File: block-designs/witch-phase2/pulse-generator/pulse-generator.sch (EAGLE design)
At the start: 87 parts, among them IC1 74LVC1G17DBV, IC10 74LVC1G08DBV, IC11 74LVC1G08DBV, IC12 741G175, IC13 741G175, IC14 741G175, IC15 741G175, IC16 741G175, IC17 74LVC1G04DBV, IC18 74LVC1G04DBV, IC19 74LVC1G08DBV, IC2 74LVC1G17DBV, IC20 74LVC1G04DBV, IC21 74LVC1G08DBV, IC22 741G175, IC23 74LVC1G08DBV, IC3 74LVC1G17DBV, IC4 NE555D, IC5 741G175, IC6 74LVC1G04DBV, IC7 74LVC1G04DBV, IC8 741G175, IC9 741G175, Q1 MMBT2222A, Q2 MMBT2222A, Q3 MMBT2222A, Q4 MMBT2222A, Q5 MMBT2222A, Q6 MMBT2907ALT1SMD

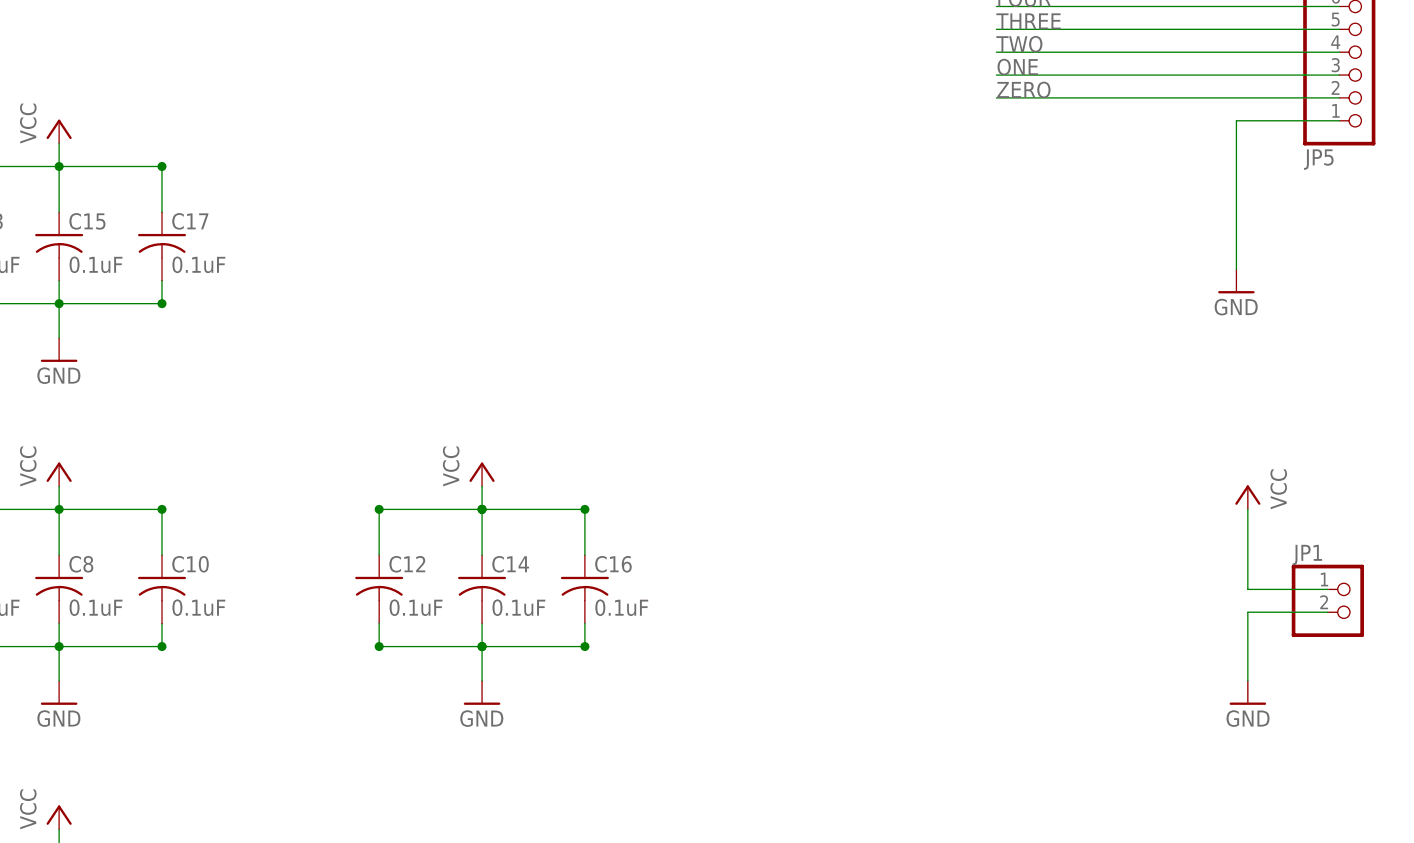
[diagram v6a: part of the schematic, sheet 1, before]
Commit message: pcb layout and labeling cleanup
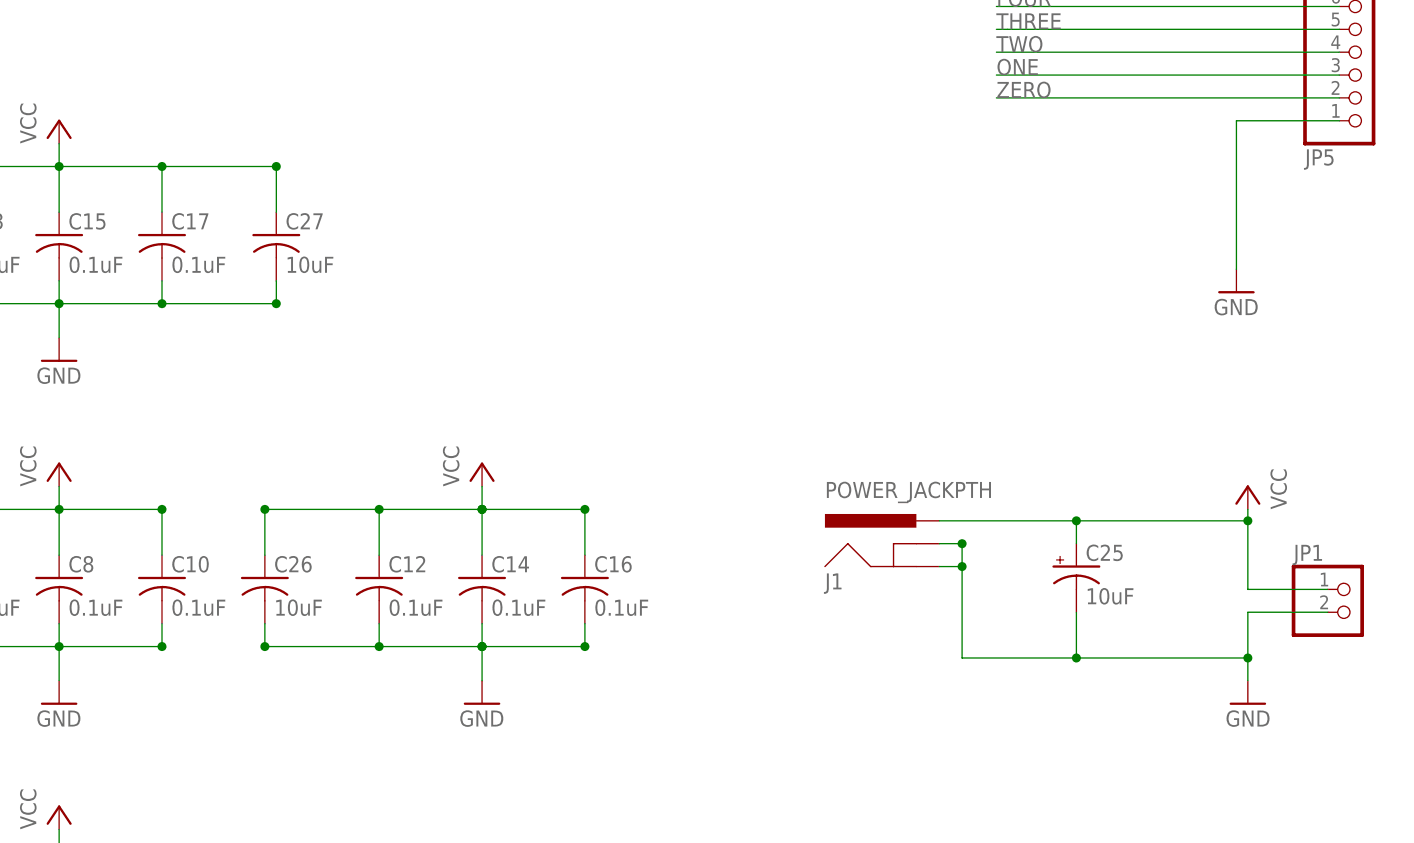
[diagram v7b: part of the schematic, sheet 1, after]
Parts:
- added C25: 10uF, SparkFun-Capacitors:10UF-16V-10%(TANT)
- added C26, C27: 10uF, resistor:C-USC0805
- added J1: POWER_JACKPTH, SparkFun-Connectors:POWER_JACKPTH
- C13: device resistor:C-USC0805 -> resistor:C-USC0603
- JP1: device pinhead:PINHD-1X2 -> custom-pinhead:PINHD-1X2
- JP2, JP4: device pinhead:PINHD-1X4 -> custom-pinhead:PINHD-1X4
- JP3: device pinhead:PINHD-1X11 -> custom-pinhead:PINHD-1X11
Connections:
- net !EXE: now also IC3A.I; no longer IC3G$1.I
- net !RST: now also IC3A.O; no longer IC3G$1.O
- net ADD/COMP: now also IC1A.O; no longer IC1G$1.O
- net CLR: now also IC2A.O; no longer IC2G$1.O
- net GND: now also C25.-, C26.2, C27.2, J1.GND, J1.GNDBREAK
- net N$18: now also IC1A.I; no longer IC1G$1.I
- net N$19: now also IC2A.I; no longer IC2G$1.I
- net VCC: now also C25.+, C26.1, C27.1, J1.PWR
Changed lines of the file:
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@@
 <layer number="112" name="tSilk" color="7" fill="1" visible="yes" active="yes"/>
 <layer number="113" name="IDFDebug" color="4" fill="1" visible="yes" active="yes"/>
+<layer number="114" name="Badge_Outline" color="7" fill="1" visible="yes" active="yes"/>
+<layer number="115" name="ReferenceISLANDS" color="7" fill="1" visible="yes" active="yes"/>
 <layer number="116" name="Patch_BOT" color="9" fill="4" visible="yes" active="yes"/>
 <layer number="118" name="Rect_Pads" color="7" fill="1" visible="no" active="no"/>
@@
 <part name="P+12" library="supply1" deviceset="VCC" device=""/>
 <part name="C16" library="resistor" deviceset="C-US" device="C0603" value="0.1uF"/>
-<part name="JP1" library="pinhead" deviceset="PINHD-1X2" device=""/>
+<part name="JP1" library="custom-pinhead" deviceset="PINHD-1X2" device=""/>
 <part name="C3" library="resistor" deviceset="C-US" device="C0603" value="0.1uF"/>
 <part name="C5" library="resistor" deviceset="C-US" device="C0603" value="0.1uF"/>
@@
 <part name="P+8" library="supply1" deviceset="VCC" device=""/>
 <part name="C11" library="resistor" deviceset="C-US" device="C0603" value="0.1uF"/>
-<part name="C13" library="resistor" deviceset="C-US" device="C0805" value="0.1uF"/>
+<part name="C13" library="resistor" deviceset="C-US" device="C0603" value="0.1uF"/>
 <part name="GND13" library="supply1" deviceset="GND" device=""/>
 <part name="P+11" library="supply1" deviceset="VCC" device=""/>
@@
 <part name="IC1" library="74xx-little-us" deviceset="74*1G17" device="DBV" technology="LVC"/>
 <part name="IC3" library="74xx-little-us" deviceset="74*1G17" device="DBV" technology="LVC"/>
-<part name="JP3" library="pinhead" deviceset="PINHD-1X11" device=""/>
+<part name="JP3" library="custom-pinhead" deviceset="PINHD-1X11" device=""/>
 <part name="GND18" library="supply1" deviceset="GND" device=""/>
-<part name="JP2" library="pinhead" deviceset="PINHD-1X4" device=""/>
+<part name="JP2" library="custom-pinhead" deviceset="PINHD-1X4" device=""/>
 <part name="P+15" library="supply1" deviceset="VCC" device=""/>
 <part name="IC20" library="74xx-little-us" deviceset="74*1G04" device="DBV" technology="LVC"/>
@@
 <part name="Q5" library="SparkFun-DiscreteSemi" deviceset="TRANSISTOR_NPN" device="MMBT2222A" value="MMBT2222A"/>
 <part name="GND19" library="supply1" deviceset="GND" device=""/>
-<part name="JP4" library="pinhead" deviceset="PINHD-1X4" device=""/>
+<part name="JP4" library="custom-pinhead" deviceset="PINHD-1X4" device=""/>
 <part name="P+16" library="supply1" deviceset="VCC" device=""/>
 <part name="D1" library="diode" deviceset="MBR0520LT" device=""/>
@@
 <part name="GND5" library="supply1" deviceset="GND" device=""/>
 <part name="P+3" library="supply1" deviceset="VCC" device=""/>
+<part name="J1" library="SparkFun-Connectors" deviceset="POWER_JACK" device="PTH"/>
+<part name="C25" library="SparkFun-Capacitors" deviceset="10UF-16V-10%(TANT)" device="" value="10uF"/>
+<part name="C26" library="resistor" deviceset="C-US" device="C0805" value="10uF"/>
+<part name="C27" library="resistor" deviceset="C-US" device="C0805" value="10uF"/>
 </parts>
 <sheets>
@@
 <instance part="P+11" gate="VCC" x="238.76" y="113.03"/>
 <instance part="C15" gate="G$1" x="238.76" y="100.33"/>
-<instance part="IC1" gate="G$1" x="74.93" y="250.19"/>
-<instance part="IC2" gate="G$1" x="74.93" y="203.2"/>
-<instance part="IC3" gate="G$1" x="74.93" y="146.05"/>
+<instance part="IC1" gate="A" x="74.93" y="250.19"/>
+<instance part="IC2" gate="A" x="74.93" y="203.2"/>
+<instance part="IC3" gate="A" x="74.93" y="146.05"/>
 <instance part="JP3" gate="A" x="383.54" y="196.85"/>
 <instance part="GND18" gate="1" x="373.38" y="226.06"/>
@@
 <instance part="GND5" gate="1" x="57.15" y="130.81"/>
 <instance part="P+3" gate="VCC" x="57.15" y="163.83"/>
+<instance part="J1" gate="G$1" x="334.01" y="60.96"/>
+<instance part="C25" gate="G$1" x="351.79" y="63.5" smashed="yes">
+<attribute name="NAME" x="352.806" y="64.135" size="1.778" layer="95"/>
+<attribute name="VALUE" x="352.806" y="59.309" size="1.778" layer="96"/>
+</instance>
+<instance part="C26" gate="G$1" x="261.62" y="62.23"/>
+<instance part="C27" gate="G$1" x="262.89" y="100.33"/>
 </instances>
 <busses>
@@
 <net name="VCC" class="0">
 <segment>
-<wire x1="370.84" y1="60.96" x2="370.84" y2="69.85" width="0.1524" layer="91"/>
+<wire x1="370.84" y1="60.96" x2="370.84" y2="68.58" width="0.1524" layer="91"/>
 <pinref part="P+14" gate="VCC" pin="VCC"/>
 <pinref part="JP1" gate="G$1" pin="1"/>
+<wire x1="370.84" y1="68.58" x2="370.84" y2="69.85" width="0.1524" layer="91"/>
 <wire x1="370.84" y1="60.96" x2="379.73" y2="60.96" width="0.1524" layer="91"/>
+<wire x1="351.79" y1="66.04" x2="351.79" y2="68.58" width="0.1524" layer="91"/>
+<pinref part="C25" gate="G$1" pin="+"/>
+<pinref part="J1" gate="G$1" pin="PWR"/>
+<wire x1="336.55" y1="68.58" x2="351.79" y2="68.58" width="0.1524" layer="91"/>
+<junction x="351.79" y="68.58"/>
+<wire x1="351.79" y1="68.58" x2="370.84" y2="68.58" width="0.1524" layer="91"/>
+<junction x="370.84" y="68.58"/>
 </segment>
 <segment>
@@
 <junction x="274.32" y="69.85"/>
 <junction x="297.18" y="69.85"/>
+<pinref part="C26" gate="G$1" pin="1"/>
+<wire x1="261.62" y1="64.77" x2="261.62" y2="69.85" width="0.1524" layer="91"/>
+<wire x1="274.32" y1="69.85" x2="261.62" y2="69.85" width="0.1524" layer="91"/>
+<junction x="261.62" y="69.85"/>
 </segment>
 <segment>
@@
 <pinref part="P+11" gate="VCC" pin="VCC"/>
 <wire x1="238.76" y1="107.95" x2="238.76" y2="110.49" width="0.1524" layer="91"/>
+<pinref part="C27" gate="G$1" pin="1"/>
+<wire x1="262.89" y1="102.87" x2="262.89" y2="107.95" width="0.1524" layer="91"/>
+<wire x1="250.19" y1="107.95" x2="262.89" y2="107.95" width="0.1524" layer="91"/>
+<junction x="262.89" y="107.95"/>
 </segment>
 </net>
@@
 <pinref part="GND17" gate="1" pin="GND"/>
 <pinref part="JP1" gate="G$1" pin="2"/>
-<wire x1="370.84" y1="58.42" x2="370.84" y2="50.8" width="0.1524" layer="91"/>
+<wire x1="370.84" y1="58.42" x2="370.84" y2="53.34" width="0.1524" layer="91"/>
+<wire x1="370.84" y1="53.34" x2="370.84" y2="50.8" width="0.1524" layer="91"/>
 <wire x1="370.84" y1="58.42" x2="379.73" y2="58.42" width="0.1524" layer="91"/>
+<wire x1="351.79" y1="58.42" x2="351.79" y2="53.34" width="0.1524" layer="91"/>
+<pinref part="C25" gate="G$1" pin="-"/>
+<wire x1="370.84" y1="53.34" x2="351.79" y2="53.34" width="0.1524" layer="91"/>
+<pinref part="J1" gate="G$1" pin="GNDBREAK"/>
+<wire x1="336.55" y1="66.04" x2="339.09" y2="66.04" width="0.1524" layer="91"/>
+<wire x1="339.09" y1="66.04" x2="339.09" y2="63.5" width="0.1524" layer="91"/>
+<pinref part="J1" gate="G$1" pin="GND"/>
+<wire x1="339.09" y1="63.5" x2="339.09" y2="53.34" width="0.1524" layer="91"/>
+<wire x1="336.55" y1="63.5" x2="339.09" y2="63.5" width="0.1524" layer="91"/>
+<junction x="339.09" y="66.04"/>
+<junction x="339.09" y="63.5"/>
+<wire x1="351.79" y1="53.34" x2="339.09" y2="53.34" width="0.1524" layer="91"/>
+<junction x="351.79" y="53.34"/>
+<junction x="370.84" y="53.34"/>
 </segment>
 <segment>
@@
 <junction x="274.32" y="54.61"/>
 <junction x="297.18" y="54.61"/>
+<pinref part="C26" gate="G$1" pin="2"/>
+<wire x1="261.62" y1="57.15" x2="261.62" y2="54.61" width="0.1524" layer="91"/>
+<wire x1="274.32" y1="54.61" x2="261.62" y2="54.61" width="0.1524" layer="91"/>
+<junction x="261.62" y="54.61"/>
 </segment>
 <segment>
@@
 <pinref part="GND13" gate="1" pin="GND"/>
 <wire x1="238.76" y1="88.9" x2="238.76" y2="92.71" width="0.1524" layer="91"/>
+<pinref part="C27" gate="G$1" pin="2"/>
+<wire x1="262.89" y1="95.25" x2="262.89" y2="92.71" width="0.1524" layer="91"/>
+<wire x1="250.19" y1="92.71" x2="262.89" y2="92.71" width="0.1524" layer="91"/>
+<junction x="262.89" y="92.71"/>
 </segment>
 </net>
@@
 </segment>
 <segment>
-<pinref part="IC3" gate="G$1" pin="O"/>
+<pinref part="IC3" gate="A" pin="O"/>
 <wire x1="85.09" y1="146.05" x2="101.6" y2="146.05" width="0.1524" layer="91"/>
 <label x="88.9" y="146.05" size="1.778" layer="95"/>
@@
 </segment>
 <segment>
-<pinref part="IC1" gate="G$1" pin="O"/>
+<pinref part="IC1" gate="A" pin="O"/>
 <wire x1="85.09" y1="250.19" x2="101.6" y2="250.19" width="0.1524" layer="91"/>
 <label x="88.9" y="250.19" size="1.778" layer="95"/>
@@
 </segment>
 <segment>
-<pinref part="IC2" gate="G$1" pin="O"/>
+<pinref part="IC2" gate="A" pin="O"/>
 <wire x1="85.09" y1="203.2" x2="101.6" y2="203.2" width="0.1524" layer="91"/>
 <label x="90.17" y="203.2" size="1.778" layer="95"/>
@@
 </segment>
 <segment>
-<pinref part="IC3" gate="G$1" pin="I"/>
+<pinref part="IC3" gate="A" pin="I"/>
 <wire x1="64.77" y1="146.05" x2="57.15" y2="146.05" width="0.1524" layer="91"/>
 <label x="27.94" y="146.05" size="1.778" layer="95"/>
@@
 <segment>
 <pinref part="D1" gate="G$1" pin="C"/>
-<pinref part="IC1" gate="G$1" pin="I"/>
+<pinref part="IC1" gate="A" pin="I"/>
 <wire x1="45.72" y1="250.19" x2="57.15" y2="250.19" width="0.1524" layer="91"/>
 <pinref part="D2" gate="G$1" pin="C"/>
@@
 <junction x="57.15" y="196.85"/>
 <pinref part="R6" gate="G$1" pin="2"/>
-<pinref part="IC2" gate="G$1" pin="I"/>
+<pinref part="IC2" gate="A" pin="I"/>
 </segment>
 </net>
@@
 <pinref part="IC18" gate="A" pin="I"/>
 <wire x1="187.96" y1="91.44" x2="212.09" y2="91.44" width="0.1524" layer="91"/>
-</segment>
-</net>
+<label x="201.93" y="91.44" size="1.778" layer="95"/>
+</segment>
+</net>

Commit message: add revision numbers
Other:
- note added: "R2"
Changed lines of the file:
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@@
 <sheet>
 <plain>
+<text x="393.7" y="7.62" size="1.778" layer="94">R2</text>
 </plain>
 <instances>
@@
 <sheet>
 <plain>
+<text x="393.7" y="7.62" size="1.778" layer="94">R2</text>
 </plain>
 <instances>
